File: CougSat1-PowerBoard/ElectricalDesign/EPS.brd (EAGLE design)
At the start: 90.4 x 95.8 mm, 416 parts, among them J1 Deployable 0, J11 CougSat Card, J2 PV1, J3 PV2, J5 SWD, J6 Umbilical, J7 PV0, J8 PV3, J9 Deployable 1, Q1 DMN53D0LDW, Q2 CSD25402Q3A, Q3 CSD25402Q3A, Q37 CSD25402Q3A, Q4 DMN2008LFU, Q5 CSD25402Q3A, Q6 DMN53D0LDW, Q8 DMN2008LFU, SW1 ESE24MH1, U1 TPS64200, U10 AD7689, U11 STM32L476RGT, U12 AD7689, U13 AD7291, U14 AD7291, U15 AD8515, U16 TPS64200, U17 AD8515, U18 INA199C1, U19 INA199C1, U2 AD7291, U20 BQ29700, U21 INA199C2, U22 INA199C1, U23 INA199C1, U24 INA199C1, U25 INA199C1, U26 TPS2115A, U27 TPS2115A, U28 TPS2115A, U29 TPS2115A, U3 AD7689, U30 TPS2115A, U31 TPS2115A, U32 TPS2115A, U33 TPS2115A, U34 TPS2115A, U35 TPS2115A, U36 TPS2115A, U37 TPS2115A, U38 TPS2115A, U39 TPS2115A, U4 TXS0102DQM, U40 TPS2115A, U41 TPS2115A, U42 TPS2115A, U43 TPS2115A, U44 TPS2115A, U45 TPS2115A, U46 TPS2115A, U47 TPS2115A, U48 TPS2115A, U49 TPS2115A, U5 TXS0102DQM, U50 TPS2115A, U51 AD8515, U52 TPS2115A, U53 TXS0102DQM, U54 TXS0102DQM, U55 TXS0102DQM, U6 BQ29700, U7 AD7291, U8 INA199C2, U9 AD7291, Y1 32.768kHz ±10ppm, Y2 8MHz ±10ppm

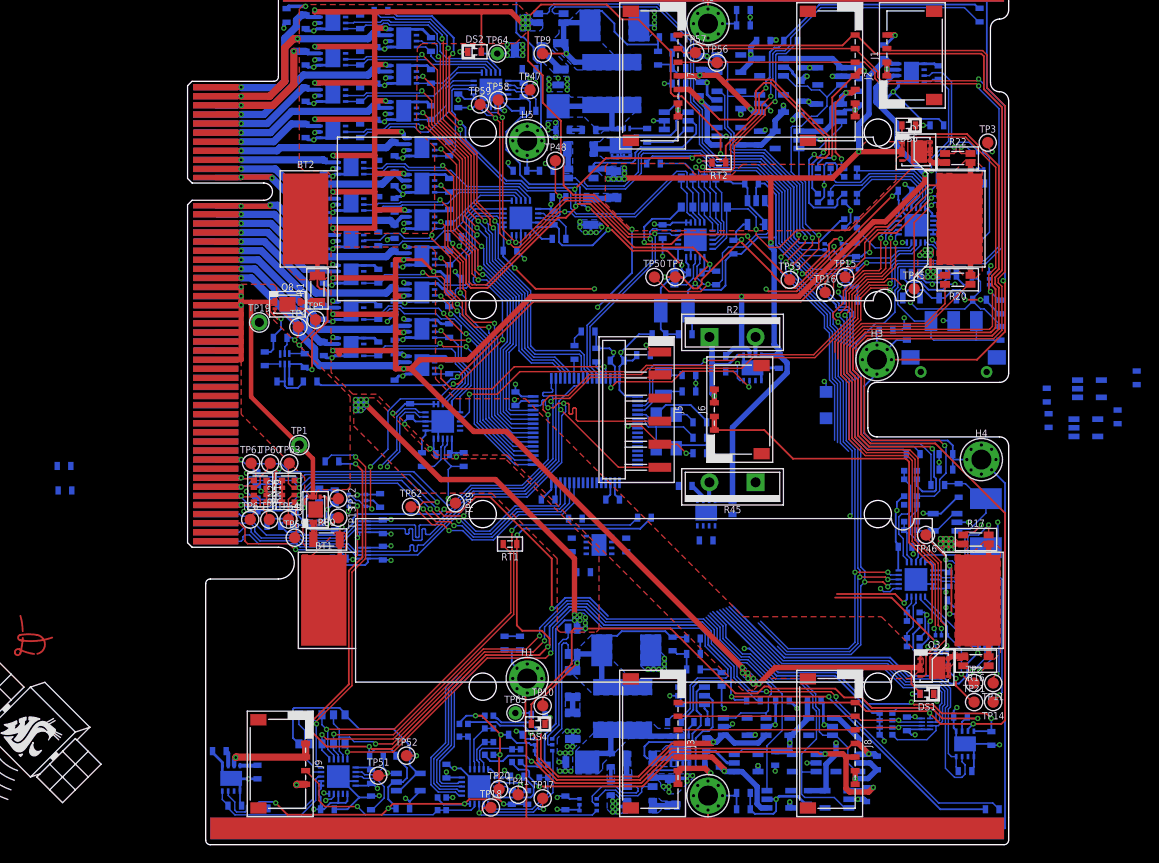
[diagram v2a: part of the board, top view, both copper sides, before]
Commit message: Laid out remaining signals
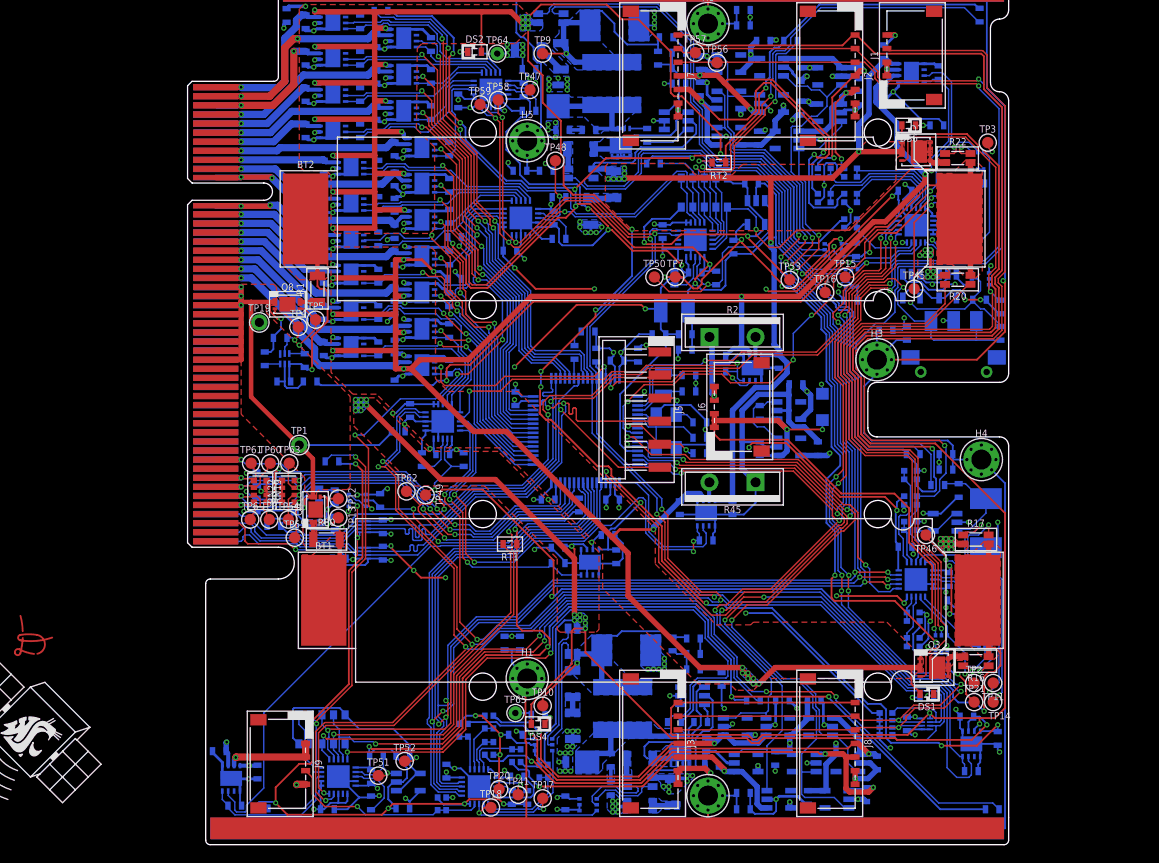
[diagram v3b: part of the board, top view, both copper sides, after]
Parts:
- moved R46 70.0 mm to (54.8, 6.60), turned to 0 degrees
- moved C60 37.5 mm to (67.0, 2.80), turned to 0 degrees
- moved R47 37.0 mm to (23.2, -2.40)
- moved D25 33.2 mm to (66.2, -0.10)
- moved C61 33.2 mm to (69.4, -4.30)
- moved D26 32.8 mm to (66.2, -4.10)
- moved C59 32.0 mm to (63.0, -4.30)
- moved R114 31.7 mm to (63.0, -0.30)
- moved R120 7.76 mm to (40.8, -16.9), turned to 0 degrees
- moved RT5 7.33 mm to (43.1, -10.5), turned to 90 degrees
- moved C65 6.16 mm to (47.2, -16.2), turned to 270 degrees
- moved C64 4.15 mm to (46.3, -13.8), turned to 180 degrees
- moved C66 3.89 mm to (40.8, -15.2), turned to 0 degrees
- moved TP49 3.42 mm to (26.2, -9.40)
- moved C73 2.47 mm to (54.2, -10.8), turned to 270 degrees
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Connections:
- removed net N$2: U7.3
- removed net N$3: U7.4
- removed net N$4: U7.5
- net !PC_3.3V-PV: now also U11.20
- net !PC_BH-1: now also U11.17
- net !PC_DEPLOY-0: now also U11.9
- net !PC_DEPLOY-1: now also U11.25
- net ADC_SEL-0: now also U11.24
- net ADC_SEL-2: now also U11.10
- net I_3.3V: now also U7.4
- net I_3.3V-PV: now also U7.5
- net I_BH-1: now also U7.3
- net PC_3.3V-5: now also U11.26
- net PC_PV-0/2A: now also U11.16
- net PC_PV-0/2B: now also U11.15
- net PC_PV-1/3A: now also U11.11
- net PC_PV-1/3B: now also U11.14
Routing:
- net PGND: track 979.6 -> 1146.2 mm, vias 122 -> 124
- net DGND: track 333.1 -> 468.7 mm, vias 20 -> 27
- net I2C_SDA: track 110.1 -> 225.8 mm, vias 5 -> 8
- net I2C_SCL: track 112.0 -> 224.7 mm, vias 5 -> 8
- net AVDD: track 237.4 -> 345.4 mm, vias 18 -> 22
- net 3.3V: track 320.4 -> 421.4 mm, vias 22 -> 29
- net SPI_MOSI: track 81.0 -> 156.0 mm, vias 4 -> 6
- net SPI_MISO: track 84.9 -> 157.5 mm, vias 4 -> 7
- net SPI_SCK: track 84.0 -> 154.9 mm
- net VBATT-B: track 261.3 -> 325.7 mm, vias 24 -> 26
- net !PC_DEPLOY-1: track 4.41 -> 64.0 mm
- net 3.3V-A: track 244.5 -> 303.0 mm, vias 24 -> 28
- net I_3.3V-PV: track 38.1 -> 95.1 mm, vias 0 -> 2
- net VBATT-A: track 260.2 -> 315.8 mm, vias 16 -> 17
- net PV_I2C_SCL: track 107.0 -> 162.2 mm, vias 3 -> 7
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
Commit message: Adjusted trace layout and polygons
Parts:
- moved LOGO2 99.1 mm to (81.0, -40.5)
- moved LOGO1 38.5 mm to (19.7, -24.7), flipped to the bottom
- moved RT12 1.14 mm to (16.6, -4.80)
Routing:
- net DB3: track 0.00 -> 48.4 mm
- net DB: track 0.00 -> 48.4 mm
- net PGND: track 1146.2 -> 1160.6 mm, vias 124 -> 136
- net DB5: track 0.00 -> 7.14 mm
- net DB4: track 0.00 -> 7.14 mm
- net VBATT-B: track 325.7 -> 331.7 mm, vias 26 -> 29
- net !VBATT_EN: track 97.2 -> 92.3 mm
- net 3.3V-B: track 233.8 -> 238.4 mm, vias 31 -> 35
- net PR_3.3V-0: track 72.1 -> 76.3 mm
- net I2C_SCL: track 224.7 -> 228.3 mm
- net I_BATT_IN-A_P: track 54.7 -> 51.6 mm
- net VBATT_EN: track 37.0 -> 40.0 mm
- net I_BATT_IN-A_N: track 55.8 -> 53.1 mm
- net 3.3V: track 421.4 -> 424.0 mm
- net CHASSIS: track 382.1 -> 384.3 mm
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- added copper zone on layer 15, net 3.3V
- added copper zone on layer 15, net 3.3V-A
- added copper zone on layer 2, net 3.3V-A
- added copper zone on layer 2, net AGND
- added copper zone on layer 15, net AVDD
- added copper zone on layer 15, net BALANCING-2
- added copper zone on layer 2, net BALANCING-2
- added copper zone on layer 1, net BALANCING-TOP
- added copper zone on layer 16, net BALANCING-TOP
- added copper zone on layer 1, net BP_VSS_I-A
- added copper zone on layer 1, net CHASSIS
- added copper zone on layer 15, net CHASSIS
- added copper zone on layer 16, net CHASSIS
- added copper zone on layer 2, net CHASSIS
- added copper zone on layer 2, net DB
- added copper zone on layer 2, net DB1
- added copper zone on layer 15, net DB2
- added copper zone on layer 15, net DB3
- added copper zone on layer 2, net DGND
- added copper zone on layer 15, net PGND
- added copper zone on layer 2, net PGND
- added copper zone on layer 16, net PR_3.3V-0
- added copper zone on layer 16, net PR_3.3V-1
- added copper zone on layer 16, net PR_3.3V-10
- added copper zone on layer 16, net PR_3.3V-11
- added copper zone on layer 16, net PR_3.3V-12
- added copper zone on layer 16, net PR_3.3V-2
- added copper zone on layer 16, net PR_3.3V-3
- added copper zone on layer 16, net PR_3.3V-4
- added copper zone on layer 16, net PR_3.3V-5
- added copper zone on layer 16, net PR_3.3V-6
- added copper zone on layer 16, net PR_3.3V-7
- added copper zone on layer 16, net PR_3.3V-8
- added copper zone on layer 16, net PR_3.3V-9
- added copper zone on layer 16, net PR_BATT-0
- added copper zone on layer 16, net PR_BATT-1
- added copper zone on layer 16, net PR_BATT-2
- added copper zone on layer 16, net PR_BATT-3
- added copper zone on layer 16, net PR_BATT-4
- added copper zone on layer 16, net PR_BATT-5
- added copper zone on layer 16, net PR_BATT-6
- added copper zone on layer 1, net PR_DEPLOY-0
- added copper zone on layer 1, net PR_DEPLOY-1
- added copper zone on layer 1, net UMB_IN

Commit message: Placed reference designators
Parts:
- removed C141, C149, C157, C163: 10µF 10%, CougsInSpace-Capacitors:1608
- removed C142, C145, C146, C150, C151, C158, C159, C164, C165, C169, C170, C171, C172, C173, C174: 100nF 10%, CougsInSpace-Capacitors:1608
- removed C148, C156, C162, C166: 1µF 10%, CougsInSpace-Capacitors:1608
- removed D24, D25, D26: MAX40200, CougsInSpace-DiscreteSemi:SOT23-5
- removed DS6: Green, CougsInSpace-LEDs:1608-POL
- removed J11: CougSat Card, CougsInSpace-Boards:CARD-FULL-OPEN+X
- removed Q37: CSD25402Q3A, CougsInSpace-DiscreteSemi:SON-3333
- removed R101: 150Ω 1%, CougsInSpace-Resistors:1608
- removed R102, R103, R90, R99: 0Ω <20mΩ, CougsInSpace-Resistors:1608
- removed R110: 10mΩ 1%, CougsInSpace-Resistors:3216
- removed R111: 12mΩ 1%, CougsInSpace-Resistors:3216-KELVIN
- removed R118: 1kΩ 0.1%, CougsInSpace-Resistors:1608
- removed R121, R122, R124, R126, R89: 2.2kΩ 1%, CougsInSpace-Resistors:1608
- removed R87: 620kΩ 1%, CougsInSpace-Resistors:1608
- removed R92: 360kΩ 1%, CougsInSpace-Resistors:1608
- removed RN22: 10kΩ 1%, CougsInSpace-Resistors:1632
- removed TP45, TP47, TP48, TP50, TP53, TP56, TP57, TP58, TP59, TP60, TP61: TEST_POINT-SMD-C-1.25, CougsInSpace-Connectors:SMD-C-1.25
- removed TP64: TEST_POINT-THT-0.7, CougsInSpace-Connectors:THT-0.7
- added C100, C104, C106, C109, C75, C76, C77, C81, C83, C90: 100nF 10%, CougsInSpace-Capacitors:1608
- added C101, C102, C110, C74, C78, C79, C82, C84, C86, C88: 10µF 10%, CougsInSpace-Capacitors:1608
- added C80: 4.7µF 10%, CougsInSpace-Capacitors:4028-POL
- added C85: 1µF 10%, CougsInSpace-Capacitors:1608
- added C99: 10µF 10%, CougsInSpace-Capacitors:3216
- added D2, D5: MAX40200, CougsInSpace-DiscreteSemi:SOT23-5
- added D6: MBRM120LT, CougsInSpace-DiscreteSemi:POWERMITE
- added DS5: Green, CougsInSpace-LEDs:1608-POL
- added J4: Umbilical, CougsInSpace-Connectors:PICOLOCK1.5-04
- added Q7: DMN53D0LDW, CougsInSpace-DiscreteSemi:SOT363
- added R27: 330Ω 1%, CougsInSpace-Resistors:1608
- added R28, R30, R40: 4.75MΩ 1%, CougsInSpace-Resistors:1608
- added R34, R44, R48, R66, R75: 0Ω <20mΩ, CougsInSpace-Resistors:1608
- added R42, R49: 1kΩ 0.1%, CougsInSpace-Resistors:1608
- added R51, R54: 2.2kΩ 1%, CougsInSpace-Resistors:1608
- added R64: 10mΩ 1%, CougsInSpace-Resistors:3216
- added R82: 12mΩ 1%, CougsInSpace-Resistors:3216-KELVIN
- added RN21: 5kΩ 0.1%, CougsInSpace-Resistors:1616
- added TP25, TP26, TP27, TP28, TP32, TP33, TP34, TP35, TP36, TP40, TP42, TP43: TEST_POINT-SMD-C-1.25, CougsInSpace-Connectors:SMD-C-1.25
- C1, C13, C16, C2, C32, C40: value 10µF 10% -> 100nF 10%; device CougsInSpace-Capacitors:3216 -> CougsInSpace-Capacitors:1608
- C10, C36: value 8pF ±0.25 -> 100nF 10%
- C105, C11, C26, C3: value 100nF 10% -> 10µF 10%; device CougsInSpace-Capacitors:1608 -> CougsInSpace-Capacitors:3216
- C108, C111, C115, C7, C70, C93, C96: value 100nF 10% -> 10µF 10%
- C112, C117, C18, C23, C29, C6, C67, C9: value 100nF 10% -> 1µF 10%
- C114, C12: value 100nF 10% -> 470pF 1%
- C116, C119, C123, C125, C126, C128, C134, C20: value 10µF 10% -> 1µF 10%
- C121, C122, C132, C136, C139, C24, C64: value 10µF 10% -> 100nF 10%
- C129: value 10µF 10% -> 4.7pF ±0.1
- C131, C133: device CougsInSpace-Capacitors:1608 -> CougsInSpace-Capacitors:3216
- C137: value 15pF 1% -> 220µF 10%; device CougsInSpace-Capacitors:1608 -> CougsInSpace-Capacitors:7132-POL
- C138: value 15pF 1% -> 10µF 10%
- C15: value 4.7pF ±0.1 -> 100nF 10%
- C17: value 220µF 10% -> 1µF 10%; device CougsInSpace-Capacitors:7132-POL -> CougsInSpace-Capacitors:1608
- C21: value 10nF 10% -> 10µF 10%
- C30: value 4.7pF ±0.1 -> 1µF 10%
- C31: value 220µF 10% -> 10µF 10%; device CougsInSpace-Capacitors:7132-POL -> CougsInSpace-Capacitors:3216
- C33: value 10µF 10% -> 220µF 10%; device CougsInSpace-Capacitors:3216 -> CougsInSpace-Capacitors:7132-POL
- C34: value 100nF 10% -> 4.7pF ±0.1
- C37: value 470pF 1% -> 100nF 10%
- C39: device CougsInSpace-Capacitors:3216 -> CougsInSpace-Capacitors:1608
- C4: value 4.7µF 10% -> 100nF 10%; device CougsInSpace-Capacitors:4028-POL -> CougsInSpace-Capacitors:1608
- C43, C44, C46, C48, C49, C50, C51, C52, C53, C54, C55, C58: value 1µF 10% -> 100nF 10%
- C45, C56: value 1µF 10% -> 10µF 10%
- C47: value 1µF 10% -> 220µF 10%; device CougsInSpace-Capacitors:1608 -> CougsInSpace-Capacitors:7132-POL
- C5: value 470pF 1% -> 1µF 10%
- C59: value 1µF 10% -> 10nF 10%
- C62: value 220µF 10% -> 8pF ±0.25; device CougsInSpace-Capacitors:7132-POL -> CougsInSpace-Capacitors:1608
- C63: value 100nF 10% -> 8pF ±0.25
- C66, C69: value 100nF 10% -> 15pF 1%
- D1, D8: value MBRM120LT -> MAX40200; device CougsInSpace-DiscreteSemi:POWERMITE -> CougsInSpace-DiscreteSemi:SOT23-5
- D12: value MAX40200 -> SS1FH10; device CougsInSpace-DiscreteSemi:SOT23-5 -> CougsInSpace-DiscreteSemi:DO-219AB
- D18: value MAX40200 -> MBRM120LT; device CougsInSpace-DiscreteSemi:SOT23-5 -> CougsInSpace-DiscreteSemi:POWERMITE
- D3: value SS1FH10 -> MAX40200; device CougsInSpace-DiscreteSemi:DO-219AB -> CougsInSpace-DiscreteSemi:SOT23-5
- J2: value PV1 -> PV0
- J3: value PV2 -> PV1
- J5: value SWD -> CougSat Card; device CougsInSpace-Connectors:SMD2.54-1X06-R -> CougsInSpace-Boards:CARD-FULL-OPEN+X
- J6: value Umbilical -> SWD; device CougsInSpace-Connectors:PICOLOCK1.5-04 -> CougsInSpace-Connectors:SMD2.54-1X06-R
- J7: value PV0 -> PV2
- LOGO1: value Satellite 16mm -> SIGNATUREBRADLEY; device CougsInSpace-Aesthetics:CIS-SATELLITE-16 -> CougsInSpace-Aesthetics:SIGN-BRADLEY
- LOGO2: value SIGNATUREBRADLEY -> Satellite 16mm; device CougsInSpace-Aesthetics:SIGN-BRADLEY -> CougsInSpace-Aesthetics:CIS-SATELLITE-16
- Q1: value DMN53D0LDW -> CSD25402Q3A; device CougsInSpace-DiscreteSemi:SOT363 -> CougsInSpace-DiscreteSemi:SON-3333
- Q2, Q3: value CSD25402Q3A -> DMN2008LFU; device CougsInSpace-DiscreteSemi:SON-3333 -> CougsInSpace-DiscreteSemi:UDFN-6-B
- Q4, Q8: value DMN2008LFU -> CSD25402Q3A; device CougsInSpace-DiscreteSemi:UDFN-6-B -> CougsInSpace-DiscreteSemi:SON-3333
- R1: value 10mΩ 1% -> 12mΩ 1%; device CougsInSpace-Resistors:3216 -> CougsInSpace-Resistors:3216-KELVIN
- R10: value 0Ω <20mΩ -> 470Ω 0.5%
- R11, R61: value 1kΩ 0.1% -> 12mΩ 1%; device CougsInSpace-Resistors:1608 -> CougsInSpace-Resistors:3216-KELVIN
- R12: value 150Ω 1% -> 2.2kΩ 1%
- R13: value 2.2kΩ 1% -> 150Ω 1%
- R14: value 1kΩ 0.1% -> 10mΩ 1%; device CougsInSpace-Resistors:1608 -> CougsInSpace-Resistors:3216
- R15: value 12mΩ 1% -> 0Ω <20mΩ; device CougsInSpace-Resistors:3216-KELVIN -> CougsInSpace-Resistors:1608
- R16, R17: value 12mΩ 1% -> 1kΩ 0.1%; device CougsInSpace-Resistors:3216-KELVIN -> CougsInSpace-Resistors:1608
- R18: value 0Ω <20mΩ -> 360kΩ 1%
- R19: value 360kΩ 1% -> 0Ω <20mΩ
- R2: value 10Ω 5% -> 12mΩ 1%; device CougsInSpace-Resistors:TO-220-2 -> CougsInSpace-Resistors:3216-KELVIN
- R20: value 12mΩ 1% -> 620kΩ 1%; device CougsInSpace-Resistors:3216-KELVIN -> CougsInSpace-Resistors:1608
- R21: value 4.75MΩ 1% -> 0Ω <20mΩ
- R25: value 330Ω 1% -> 10kΩ 0.1%
- R26: value 0Ω <20mΩ -> 750Ω 0.5%
- R29: value 2.2kΩ 1% -> 10kΩ 0.1%
- R3: value 4.75MΩ 1% -> 10mΩ 1%; device CougsInSpace-Resistors:1608 -> CougsInSpace-Resistors:3216
- R31: value 620kΩ 1% -> 2.2kΩ 1%
- R37: value 1kΩ 0.1% -> 330Ω 1%
- R38, R39: value 1kΩ 0.1% -> 750Ω 0.5%
- R4: value 4.75MΩ 1% -> 10Ω 5%; device CougsInSpace-Resistors:1608 -> CougsInSpace-Resistors:TO-220-2
- R41: value 12mΩ 1% -> 2.2kΩ 1%; device CougsInSpace-Resistors:3216-KELVIN -> CougsInSpace-Resistors:1608
- R43, R62: value 2.2kΩ 1% -> 0Ω <20mΩ
- R45: value 10Ω 5% -> 750Ω 0.5%; device CougsInSpace-Resistors:TO-220-2 -> CougsInSpace-Resistors:1608
- R46: value 0Ω <20mΩ -> 4.75MΩ 1%
- R47: value 0Ω <20mΩ -> 1kΩ 0.1%
- R5: value 12mΩ 1% -> 10Ω 5%; device CougsInSpace-Resistors:3216-KELVIN -> CougsInSpace-Resistors:TO-220-2
- R50, R55, R73: value 0Ω <20mΩ -> 2.2kΩ 1%
- R56: value 330Ω 1% -> 1kΩ 0.1%
- R58: value 2.2kΩ 1% -> 750Ω 0.5%
- R60, R65: value 750Ω 0.5% -> 2.2kΩ 1%
- R67: value 750Ω 0.5% -> 1.2kΩ 0.1%
- R68: value 470Ω 0.5% -> 150Ω 1%
- R69: value 470Ω 0.5% -> 1kΩ 0.1%
- R7, R8: value 10kΩ 0.1% -> 12mΩ 1%; device CougsInSpace-Resistors:1608 -> CougsInSpace-Resistors:3216-KELVIN
- R70: value 1.2kΩ 0.1% -> 2.2kΩ 1%
- R72: value 2.2kΩ 1% -> 360kΩ 1%
- R74: value 750Ω 0.5% -> 470Ω 0.5%
- R77: value 1kΩ 0.1% -> 620kΩ 1%
- R78: value 2.2kΩ 1% -> 1kΩ 0.1%
- R79: value 4.75MΩ 1% -> 2.2kΩ 1%
- R80: value 10mΩ 1% -> 0Ω <20mΩ; device CougsInSpace-Resistors:3216 -> CougsInSpace-Resistors:1608
- R83: value 750Ω 0.5% -> 0Ω <20mΩ
- RN1, RN2, RN9: value 5kΩ 0.1% -> 10kΩ 1%; device CougsInSpace-Resistors:1616 -> CougsInSpace-Resistors:1632
- RN17, RN18: value 10kΩ 5% -> 5kΩ 0.1%; device CougsInSpace-Resistors:3264 -> CougsInSpace-Resistors:1616
- RN19: value 10kΩ 1% -> 10kΩ 5%; device CougsInSpace-Resistors:1632 -> CougsInSpace-Resistors:3264
- RN20: value 10kΩ 1% -> 5kΩ 0.1%; device CougsInSpace-Resistors:1632 -> CougsInSpace-Resistors:1616
- RN8: value 5kΩ 0.1% -> 10kΩ 5%; device CougsInSpace-Resistors:1616 -> CougsInSpace-Resistors:3264
- TP1: value TEST_POINT-THT-1.0 -> TEST_POINT-SMD-C-1.25; device CougsInSpace-Connectors:THT-1.0 -> CougsInSpace-Connectors:SMD-C-1.25
- TP17: value TEST_POINT-SMD-C-1.25 -> TEST_POINT-THT-1.0; device CougsInSpace-Connectors:SMD-C-1.25 -> CougsInSpace-Connectors:THT-1.0
- TP2: value TEST_POINT-SMD-C-1.25 -> TEST_POINT-THT-0.7; device CougsInSpace-Connectors:SMD-C-1.25 -> CougsInSpace-Connectors:THT-0.7
- U1: value TPS64200 -> INA199C1; device CougsInSpace-IC-Power:SOT23-6 -> CougsInSpace-IC-Amplifiers:SOT363
- U10: value AD7689 -> INA199C2; device CougsInSpace-IC-Conversion:QFN-20-4040 -> CougsInSpace-IC-Amplifiers:SOT363
- U11: value STM32L476RGT -> INA199C1; device CougsInSpace-IC-µController:QFP-64-1010 -> CougsInSpace-IC-Amplifiers:SOT363
- U13: value AD7291 -> INA199C2; device CougsInSpace-IC-Conversion:QFN-20-4040 -> CougsInSpace-IC-Amplifiers:SOT363
- U14, U7: value AD7291 -> TPS2115A; device CougsInSpace-IC-Conversion:QFN-20-4040 -> CougsInSpace-IC-Power:VSON-8
- U15: value AD8515 -> TXS0102DQM; device CougsInSpace-IC-Amplifiers:SOT23-5 -> CougsInSpace-IC-Comms:X2SON-8
- U16: value TPS64200 -> TXS0102DQM; device CougsInSpace-IC-Power:SOT23-6 -> CougsInSpace-IC-Comms:X2SON-8
- U18: value INA199C1 -> BQ29700; device CougsInSpace-IC-Amplifiers:SOT363 -> CougsInSpace-IC-Power:WSON-6
- U19, U24, U25: value INA199C1 -> TPS2115A; device CougsInSpace-IC-Amplifiers:SOT363 -> CougsInSpace-IC-Power:VSON-8
- U2: value AD7291 -> AD7689
- U20: value BQ29700 -> TXS0102DQM; device CougsInSpace-IC-Power:WSON-6 -> CougsInSpace-IC-Comms:X2SON-8
- U21, U8: value INA199C2 -> TXS0102DQM; device CougsInSpace-IC-Amplifiers:SOT363 -> CougsInSpace-IC-Comms:X2SON-8
- U22: value INA199C1 -> STM32L476RGT; device CougsInSpace-IC-Amplifiers:SOT363 -> CougsInSpace-IC-µController:QFP-64-1010
- U23: value INA199C1 -> AD7291; device CougsInSpace-IC-Amplifiers:SOT363 -> CougsInSpace-IC-Conversion:QFN-20-4040
- U26: value TPS2115A -> BQ29700; device CougsInSpace-IC-Power:VSON-8 -> CougsInSpace-IC-Power:WSON-6
- U3: value AD7689 -> AD8515; device CougsInSpace-IC-Conversion:QFN-20-4040 -> CougsInSpace-IC-Amplifiers:SOT23-5
- U31, U34, U44: value TPS2115A -> INA199C1; device CougsInSpace-IC-Power:VSON-8 -> CougsInSpace-IC-Amplifiers:SOT363
- U35, U39, U50: value TPS2115A -> AD7291; device CougsInSpace-IC-Power:VSON-8 -> CougsInSpace-IC-Conversion:QFN-20-4040
- U37: value TPS2115A -> AD7689; device CougsInSpace-IC-Power:VSON-8 -> CougsInSpace-IC-Conversion:QFN-20-4040
- U4, U53, U54, U55: value TXS0102DQM -> TPS2115A; device CougsInSpace-IC-Comms:X2SON-8 -> CougsInSpace-IC-Power:VSON-8
- U40: value TPS2115A -> AD8515; device CougsInSpace-IC-Power:VSON-8 -> CougsInSpace-IC-Amplifiers:SOT23-5
- U47: value TPS2115A -> TPS64200; device CougsInSpace-IC-Power:VSON-8 -> CougsInSpace-IC-Power:SOT23-6
- U5: value TXS0102DQM -> AD7291; device CougsInSpace-IC-Comms:X2SON-8 -> CougsInSpace-IC-Conversion:QFN-20-4040
- U51: value AD8515 -> TPS2115A; device CougsInSpace-IC-Amplifiers:SOT23-5 -> CougsInSpace-IC-Power:VSON-8
- U6: value BQ29700 -> INA199C1; device CougsInSpace-IC-Power:WSON-6 -> CougsInSpace-IC-Amplifiers:SOT363
- U9: value AD7291 -> TPS64200; device CougsInSpace-IC-Conversion:QFN-20-4040 -> CougsInSpace-IC-Power:SOT23-6
- Y1: value 32.768kHz ±10ppm -> 8MHz ±10ppm; device CougsInSpace-Clocks:SMD-3215 -> CougsInSpace-Clocks:SMD-5032
- Y2: value 8MHz ±10ppm -> 32.768kHz ±10ppm; device CougsInSpace-Clocks:SMD-5032 -> CougsInSpace-Clocks:SMD-3215
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- renumbered C140 to C92, C143 to C97, C152 to C94, C153 to C103, C154 to C89, C155 to C98, C160 to C95, C161 to C87, C167 to C91, C168 to C107, R114 to R36, R115 to R32, R116 to R33, R117 to R53, R120 to R24, R123 to R76, R125 to R71, R84 to R23, R85 to R57, R88 to R52, TP46 to TP30, TP49 to TP24, TP51 to TP39, TP52 to TP38, TP54 to TP29, TP55 to TP31, TP62 to TP23, TP63 to TP22, TP65 to TP37
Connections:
- net !NRST: now also C59.1, J6.5, U22.7; no longer C21.1, J5.5, U11.7
- net !PC_3.3V-0: now also U22.57, U55.3; no longer U11.57, U27.3
- net !PC_3.3V-1: now also U22.56, U54.3; no longer U11.56, U28.3
- net !PC_3.3V-10: now also U22.41, U41.3; no longer U11.41, U37.3
- net !PC_3.3V-11: now also U22.39; no longer U11.39
- net !PC_3.3V-12: now also U22.40, U36.3; no longer U11.40, U39.3
- net !PC_3.3V-2: now also U22.53, U53.3; no longer U11.53, U29.3
- net !PC_3.3V-3: now also U22.52, U51.3; no longer U11.52, U30.3
- net !PC_3.3V-4: now also U22.51, U49.3; no longer U11.51, U31.3
- net !PC_3.3V-5: now also U48.3; no longer U32.3
- net !PC_3.3V-6: now also U22.45, U46.3; no longer U11.45, U33.3
- net !PC_3.3V-7: now also U22.44, U45.3; no longer U11.44, U34.3
- net !PC_3.3V-8: now also U22.43, U43.3; no longer U11.43, U35.3
- net !PC_3.3V-9: now also U22.42, U42.3; no longer U11.42, U36.3
- net !PC_3.3V-PV: now also U22.20, U7.3; no longer U11.20, U52.3
- net !PC_BATT-0: now also U22.38, U33.3; no longer U11.38, U40.3
- net !PC_BATT-1: now also U22.37, U32.3; no longer U11.37, U41.3
- net !PC_BATT-2: now also U22.36, U30.3; no longer U11.36, U42.3
- net !PC_BATT-3: now also U22.35, U29.3; no longer U11.35, U43.3
- net !PC_BATT-4: now also U22.34, U28.3; no longer U11.34, U44.3
- net !PC_BATT-5: now also U22.33, U27.3; no longer U11.33, U45.3
- net !PC_BATT-6: now also U22.61, U25.3; no longer U11.61, U46.3
- net !PC_BH-0: now also U22.62, U24.3; no longer U11.62, U47.3
- net !PC_BH-1: now also U19.3, U22.17; no longer U11.17, U48.3
- net !PC_DEPLOY-0: now also U22.9, U52.3; no longer U11.9, U49.3
- net !PC_DEPLOY-1: now also U22.25, U4.3; no longer U11.25, U50.3
- net !VBATT_EN: now also Q1.4, Q4.4, Q7.2, Q7.3; no longer Q1.2, Q1.3, Q2.4, Q3.4
- net 3.3V: now also C1.1, C104.1, C118.1, C16.1, C42.1, C44.1, C45.1, C46.1, C51.1, C52.1, C53.1, C54.1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; no longer C145.1, C150.1, C158.1, C164.1, C172.1, C173.1, C174.1, C23.1, C25.1, C26.1, C41.1, C6.1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
- net 3.3V-A: now also C100.1, C24.1, C41.1, DS1.A, R82.2, RN16.2, U14.8, U41.8, U42.8, U43.8, U45.8, U46.8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; no longer C117.1, C65.1, C68.1, DS2.A, R41.2, RN7.2, U26.8, U27.8, U28.8, U29.8, U30.8, U31.8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
- net 3.3V-B: now also C139.1, C28.1, C43.1, R22.1, RN4.2, U14.6, U41.6, U42.6, U43.6, U45.6, U46.6, U48.6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; no longer C118.1, C66.1, C67.1, R15.1, RN12.2, U26.6, U27.6, U28.6, U29.6, U30.6, U31.6, U32.6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
- net 3.3V_I-A: now also C129.1, C131.1, C137.A, L2.2, R80.2, R82.1, TP3.1; no longer C13.1, C15.1, C17.A, L1.2, R35.2, R41.1, TP9.1
- net 3.3V_I-B: now also C31.1, C33.A, C34.1, L1.2, R22.2, TP36.1; no longer C30.1, C31.A, C33.1, L2.2, R15.2, TP10.1
- net 3.3V_ISENS-A: now also Q8.5, Q8.6, Q8.7, Q8.8, Q8.PAD, R64.1, U47.4; no longer Q5.5, Q5.6, Q5.7, Q5.8, Q5.PAD, R6.1, U1.4
- net 3.3V_ISENS-B: now also Q5.5, Q5.6, Q5.7, Q5.8, Q5.PAD, R14.1, U9.4; no longer Q37.5, Q37.6, Q37.7, Q37.8, Q37.PAD, R110.1, U16.4
- net 3.3V_LED-A: now also DS1.C, R78.2; no longer DS2.C, R38.2
- net 3.3V_LED-B: now also R16.2; no longer R77.2
- net 3.3V_REG_BUCK_NODE-A: now also D18.C, L2.1, Q8.1, Q8.2, Q8.3, R68.2; no longer D1.C, L1.1, Q5.1, Q5.2, Q5.3, R12.2
- net 3.3V_REG_BUCK_NODE-B: now also D6.C, L1.1, Q5.1, Q5.2, Q5.3, R13.2; no longer D8.C, L2.1, Q37.1, Q37.2, Q37.3, R101.2
- net 3.3V_REG_FB-A: now also C129.2, R75.2, R77.1, U47.3; no longer C15.2, R26.2, R31.1, U1.3
- net 3.3V_REG_FB-B: now also C34.2, R19.2, R20.1, U9.3; no longer C30.2, R87.1, R90.2, U16.3
- net 3.3V_REG_FBRES_HIGH-A: now also R77.2, R80.1; no longer R31.2, R35.1
- net 3.3V_REG_FBRES_HIGH-B: now also R20.2; no longer R87.2
- net 3.3V_REG_FBRES_LOW-A: now also R72.2, R75.1; no longer R19.2, R26.1
- net 3.3V_REG_FBRES_LOW-B: now also R18.2, R19.1; no longer R90.1, R92.2
- net 3.3V_REG_INCAP-A: now also C105.2, C99.1; no longer C1.2, C2.1
- net 3.3V_REG_INCAP-B: now also C11.2, C3.1; no longer C39.1, C40.2
- net 3.3V_REG_OUTCAP-A: now also C131.2, C133.1; no longer C13.2, C16.1
- net 3.3V_REG_OUTCAP-B: now also C26.1, C31.2; no longer C32.1, C33.2
- net 3.3V_REG_RSENS-A: now also R61.1, R64.2; no longer R5.1, R6.2
- net 3.3V_REG_RSENS-B: now also R11.1, R14.2; no longer R110.2, R111.1
- net 3.3V_REG_SNUBBER-A: now also C114.1, R68.1; no longer C5.1, R12.1
- net 3.3V_REG_SNUBBER-B: now also C12.1, R13.1; no longer C37.1, R101.1
- net 3.3V_REG_SW-A: now also R66.1, U47.6; no longer R9.1, U1.6
- net 3.3V_REG_SW-B: now also R15.1, U9.6; no longer R102.1, U16.6
- net 3.3V_REG_SW_GATE-A: now also Q8.4, R66.2; no longer Q5.4, R9.2
- net 3.3V_REG_SW_GATE-B: now also Q5.4, R15.2; no longer Q37.4, R102.2
- net ADC_3.3V-A: now also RN16.3, RN16.4, U37.9; no longer RN7.3, RN7.4, U10.9
- net ADC_3.3V-B: now also RN4.3, RN4.4, U2.6; no longer RN12.3, RN12.4, U3.6
- net ADC_DCAP-3: now also C116.1, U50.8; no longer C148.1, U13.8
- net ADC_DCAP-4: now also U39.8; no longer U2.8
- net ADC_DCAP-5: now also C57.1, U23.8; no longer C156.1, U7.8
- net ADC_DCAP-6: now also C85.1, U35.8; no longer C19.1, U9.8
- net ADC_DCAP-7: now also C5.1, U5.8; no longer C162.1, U14.8
- net ADC_EJECT_TIMER_BUF: now also RN13.3, RN13.4; no longer RN8.3, RN8.4
- net ADC_PV_IN-0A: now also RN17.3, RN17.4, U37.16; no longer RN2.3, RN2.4, U10.16
- net ADC_PV_IN-0B: now also RN18.3, RN18.4, U37.17; no longer RN3.3, RN3.4, U10.17
- net ADC_PV_IN-1A: now also RN21.3, RN21.4, U37.18; no longer RN4.3, RN4.4, U10.18
- net ADC_PV_IN-1B: now also RN20.3, RN20.4, U37.19; no longer RN5.3, RN5.4, U10.19
- net ADC_PV_IN-2A: now also U2.17; no longer U3.17
- net ADC_PV_IN-2B: now also RN5.3, RN5.4, U2.19; no longer RN11.3, RN11.4, U3.19
- net ADC_PV_IN-3A: now also RN7.3, RN7.4, U2.16; no longer RN13.3, RN13.4, U3.16
- net ADC_PV_IN-3B: now also RN6.3, RN6.4, U2.18; no longer RN9.3, RN9.4, U3.18
- net ADC_REF-0: now also C7.1, U2.2; no longer C24.1, U3.2
- net ADC_REF-1: now also C102.1, TP14.1, U37.2; no longer C139.1, TP45.1, U10.2
- net ADC_REF-2: now also C39.1; no longer C141.1
- net ADC_REF-3: now also C127.1, TP5.1, U50.7; no longer C149.1, TP47.1, U13.7
- net ADC_REF-4: now also TP9.1, U39.7; no longer TP48.1, U2.7
- net ADC_REF-5: now also C56.1, U23.7; no longer C157.1, U7.7
- net ADC_REF-6: now also C84.1, TP10.1, U35.7, U40.3; no longer C20.1, TP50.1, U51.3, U9.7
- net ADC_REF-7: now also C21.1, U3.3, U5.7; no longer C163.1, U14.7, U15.3
- net ADC_REFIN-0: now also C8.1, U2.3; no longer C42.1, U3.3
- net ADC_REFIN-1: now also U37.3; no longer U10.3
- net ADC_REFIN-2: now also C37.1; no longer C142.1
- net ADC_SEL-0: now also U2.11, U22.24; no longer U11.24, U3.11
- net ADC_SEL-1: now also U22.2, U37.11; no longer U10.11, U11.2
- net ADC_SEL-2: now also U22.10; no longer U11.10
- net ADC_UMB_IN: now also RN11.3, RN11.4; no longer RN14.3, RN14.4
- net ADC_VBATT-A: now also RN15.3, RN15.4; no longer RN6.3, RN6.4
- net ADC_VBATT-B: now also RN12.3, RN12.4; no longer RN1.3, RN1.4
- net AGND: now also C102.2, C106.2, C14.2, C2.2, C21.2, C25.2, C32.2, C36.2, C37.2, C38.2, C39.2, C4.2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; no longer C139.2, C141.2, C142.2, C157.2, C159.2, C163.2, C165.2, C166.2, C169.2, C170.2, C171.2, C18.2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
- net AVDD: now also C106.1, C122.1, C13.1, C14.1, C2.1, C25.1, C32.1, C36.1, C38.1, C4.1, C40.1, C58.1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; no longer C12.1, C146.1, C151.1, C159.1, C165.1, C169.1, C170.1, C171.1, C18.1, C29.1, C3.1, C34.1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
- net AVREF-0: now also RN19.10, RN19.5, TP13.1, U40.1, U40.4; no longer RN18.10, RN18.5, TP53.1, U51.1, U51.4
- net AVREF-1: now also C20.1, RN8.10, RN8.5, U3.1, U3.4; no longer C166.1, RN17.10, RN17.5, U15.1, U15.4
- net BATT_PROTECT_BAT-A: now also C68.1, R37.1, U26.5; no longer C14.1, R25.1, U6.5
- net BATT_PROTECT_BAT-B: now also C48.1, R27.1, U18.5; no longer C63.1, R56.1, U20.5
- net BATT_PROTECT_COUT-A: now also Q2.3, R46.2, TP18.1, U26.2; no longer Q8.3, R21.2, TP4.1, U6.2
- net BATT_PROTECT_COUT-B: now also Q3.4, R30.2, TP25.1, U18.2; no longer Q4.4, R79.2, TP12.1, U20.2
- net BATT_PROTECT_DOUT-A: now also Q2.4, R40.1, TP16.1, U26.3; no longer Q8.4, R3.1, TP5.1, U6.3
- net BATT_PROTECT_DOUT-B: now also Q3.3, R28.2, TP26.1, U18.3; no longer Q4.3, R4.2, TP13.1, U20.3
- net BATT_PROTECT_GND-A: now also R41.2, U26.6; no longer R29.2, U6.6
- net BATT_PROTECT_GND-B: now also R31.2, U18.6; no longer R62.2, U20.6
- net BOOT0: now also R43.2, U22.60; no longer R55.2, U11.60
- net BP_VSS-A: now also BT1.A, C68.2, R40.2, U26.4; no longer BT2.A, C14.2, R1.2, U6.4
- net BP_VSS-A1: now also BT2.A, C48.2, R28.1, R6.2, U18.4; no longer BT1.A, C63.2, R4.1, R80.2, U20.4
- net BP_VSS_I-A: now also Q2.6, R3.1; no longer Q8.6, R1.1
- net BP_VSS_I-B: now also Q3.1, R6.1; no longer Q4.1, R80.1
- net BUS_CTRL_SYNC: now also J5.A42, J5.B42, RN1.1, TP20.1, U21.3; no longer J11.A42, J11.B42, RN19.1, TP61.1, U55.3
- net BUS_I2C0_IRQ: now also J5.A45, J5.B45, RN1.4, TP27.1, U20.2; no longer J11.A45, J11.B45, RN19.4, TP6.1, U54.2
- net BUS_I2C0_SCL: now also J5.A44, J5.B44, RN1.3, TP28.1, U20.3; no longer J11.A44, J11.B44, RN19.3, TP8.1, U54.3
- net BUS_I2C0_SDA: now also J5.A43, J5.B43, RN1.2, TP21.1, U21.2; no longer J11.A43, J11.B43, RN19.2, TP60.1, U55.2
- net BUS_I2C_IRQ: now also RN2.1, U20.7, U22.28; no longer RN22.1, U11.28, U54.7
- net BUS_I2C_SCL: now also RN2.2, U20.6, U22.29; no longer RN22.2, U11.29, U54.6
- net BUS_I2C_SDA: now also RN2.3, U21.7, U22.30; no longer RN22.3, U11.30, U55.7
- net BUS_JTAG_TCK: now also J5.A46, U16.7; no longer J11.A46, U5.7
- net BUS_JTAG_TDI: now also J5.A47, U16.6; no longer J11.A47, U5.6
- net BUS_JTAG_TDO: now also J5.A48, U15.7; no longer J11.A48, U4.7
- net BUS_JTAG_TMS: now also J5.A49, U15.6; no longer J11.A49, U4.6
- net CHASSIS: now also C10.1, C109.1, C136.1, C55.1, C77.1, J5.CHASSIS@1, J5.CHASSIS@2, J5.CHASSIS@3, J5.CHASSIS@4, R21.2, R34.2, R48.2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; no longer C11.1, C22.1, C28.1, C38.1, C9.1, J11.CHASSIS@1, J11.CHASSIS@2, J11.CHASSIS@3, J11.CHASSIS@4, R10.2, R103.2, R18.2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
- net CTRL_SYNC: now also RN2.4, U21.6, U22.27; no longer RN22.4, U11.27, U55.6
- net DEPLOY_SENSE-0: now also RN14.3, RN14.4; no longer RN15.3, RN15.4
- net DEPLOY_SENSE-1: now also RN3.3, RN3.4, U2.9; no longer RN16.3, RN16.4, U3.9
- net DGND: now also C1.2, C104.2, C116.2, C118.2, C13.2, C16.2, C40.2, C42.2, C44.2, C46.2, C5.2, C51.2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; no longer C10.2, C12.2, C137.2, C138.2, C145.2, C146.2, C148.2, C150.2, C156.2, C158.2, C162.2, C164.2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
- net EJECT_TIMER: now also C47.A; no longer C62.A
- net EJECT_TIMER_BUF: now also RN13.2; no longer RN8.2
- net EJECT_TIMER_DISCHARGE: now also Q7.6; no longer Q1.6
- net I2C_SCL: now also RN9.4, TP7.1, U22.58, U23.15, U35.15, U39.15, U5.15, U50.15, U8.7; no longer RN20.4, TP59.1, U11.58, U13.15, U14.15, U2.15, U53.7, U7.15, U9.15
- net I2C_SDA: now also RN9.1, TP6.1, U22.59, U23.14, U35.14, U39.14, U5.14, U50.14, U8.6; no longer RN20.1, TP58.1, U11.59, U13.14, U14.14, U2.14, U53.6, U7.14, U9.14
- net I_3.3V: now also U14.4, U23.4; no longer U26.4, U7.4
- net I_3.3V-0: now also R81.2, U50.5, U55.4; no longer R121.2, U13.5, U27.4
- net I_3.3V-1: now also R79.2, U50.4, U54.4; no longer R122.2, U13.4, U28.4
- net I_3.3V-10: now also R59.2, U39.3, U41.4; no longer R81.2, U2.3, U37.4
- net I_3.3V-11: now also R58.2, U39.2; no longer R83.2, U2.2
- net I_3.3V-12: now also U36.4, U39.1; no longer U2.1, U39.4
- net I_3.3V-2: now also U50.3, U53.4; no longer U13.3, U29.4
- net I_3.3V-3: now also R73.2, U50.2, U51.4; no longer R124.2, U13.2, U30.4
- net I_3.3V-4: now also U49.4, U50.1; no longer U13.1, U31.4
- net I_3.3V-5: now also R70.2, U48.4, U50.20; no longer R126.2, U13.20, U32.4
- net I_3.3V-6: now also R67.2, U46.4, U50.19; no longer R70.2, U13.19, U33.4
- net I_3.3V-7: now also R65.2, U45.4, U50.18; no longer R72.2, U13.18, U34.4
- net I_3.3V-8: now also R63.2, U39.5, U43.4; no longer R74.2, U2.5, U35.4
- net I_3.3V-9: now also R60.2, U39.4, U42.4; no longer R78.2, U2.4, U36.4
- net I_3.3V-PV: now also R12.2, U23.5, U7.4; no longer R89.2, U52.4, U7.5
- net I_3.3V_IN-A: now also TP12.1, U31.6, U37.7; no longer TP15.1, U10.7, U22.6
- net I_3.3V_IN-A_N: now also R61.1-KELVIN, U31.5; no longer R5.1-KELVIN, U22.5
- net I_3.3V_IN-A_P: now also R61.2-KELVIN, U31.4; no longer R5.2-KELVIN, U22.4
- net I_3.3V_IN-B: now also TP43.1, U1.6, U2.8; no longer TP18.1, U25.6, U3.8
- net I_3.3V_IN-B_N: now also R11.1-KELVIN, U1.5; no longer R111.1-KELVIN, U25.5
- net I_3.3V_IN-B_P: now also R11.2-KELVIN, U1.4; no longer R111.2-KELVIN, U25.4
- net I_3.3V_OUT-A: now also TP15.1, U34.6, U37.8; no longer TP16.1, U10.8, U23.6
- net I_3.3V_OUT-A_N: now also R82.2-KELVIN, U34.5; no longer R41.2-KELVIN, U23.5
- net I_3.3V_OUT-A_P: now also R82.1-KELVIN, U34.4; no longer R41.1-KELVIN, U23.4
- net I_3.3V_OUT-B: now also TP42.1, U2.7, U6.6; no longer TP17.1, U24.6, U3.7
- net I_3.3V_OUT-B_N: now also R22.1-KELVIN, U6.5; no longer R15.1-KELVIN, U24.5
- net I_3.3V_OUT-B_P: now also R22.2-KELVIN, U6.4; no longer R15.2-KELVIN, U24.4
- net I_BATT-0: now also R56.2, U33.4, U39.20; no longer R11.2, U2.20, U40.4
- net I_BATT-1: now also R55.2, U32.4, U39.19; no longer R13.2, U2.19, U41.4
- net I_BATT-2: now also R54.2, U30.4, U39.18; no longer R43.2, U2.18, U42.4
- net I_BATT-3: now also R51.2, U23.1, U29.4; no longer R58.2, U43.4, U7.1
- net I_BATT-4: now also R50.2, U23.20, U28.4; no longer R59.2, U44.4, U7.20
- net I_BATT-5: now also R45.2, U23.19, U27.4; no longer R60.2, U45.4, U7.19
- net I_BATT-6: now also R39.2, U23.18, U25.4; no longer R63.2, U46.4, U7.18
- net I_BATT_IN-A: now also TP32.1, U10.6; no longer TP2.1, U8.6
- net I_BATT_IN-A_N: now also R2.1-KELVIN, U10.5; no longer R20.1-KELVIN, U8.5
- net I_BATT_IN-A_P: now also R2.2-KELVIN, U10.4; no longer R20.2-KELVIN, U8.4
- net I_BATT_IN-B: now also TP35.1, U13.6; no longer TP14.1, U21.6
- net I_BATT_IN-B_N: now also R7.2-KELVIN, U13.5; no longer R17.2-KELVIN, U21.5
- net I_BATT_IN-B_P: now also R7.1-KELVIN, U13.4; no longer R17.1-KELVIN, U21.4
- net I_BATT_OUT-A: now also TP8.1, U37.6, U44.6; no longer TP3.1, U10.6, U18.6
- net I_BATT_OUT-A_N: now also R1.1-KELVIN, U44.5; no longer R22.1-KELVIN, U18.5
- net I_BATT_OUT-A_P: now also R1.2-KELVIN, U44.4; no longer R22.2-KELVIN, U18.4
- net I_BATT_OUT-B: now also TP33.1, U11.6; no longer TP11.1, U19.6
- net I_BATT_OUT-B_N: now also R8.2-KELVIN, U11.5; no longer R16.2-KELVIN, U19.5
- net I_BATT_OUT-B_P: now also R8.1-KELVIN, U11.4; no longer R16.1-KELVIN, U19.4
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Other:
- board text added: "A"
- board text added: "B"

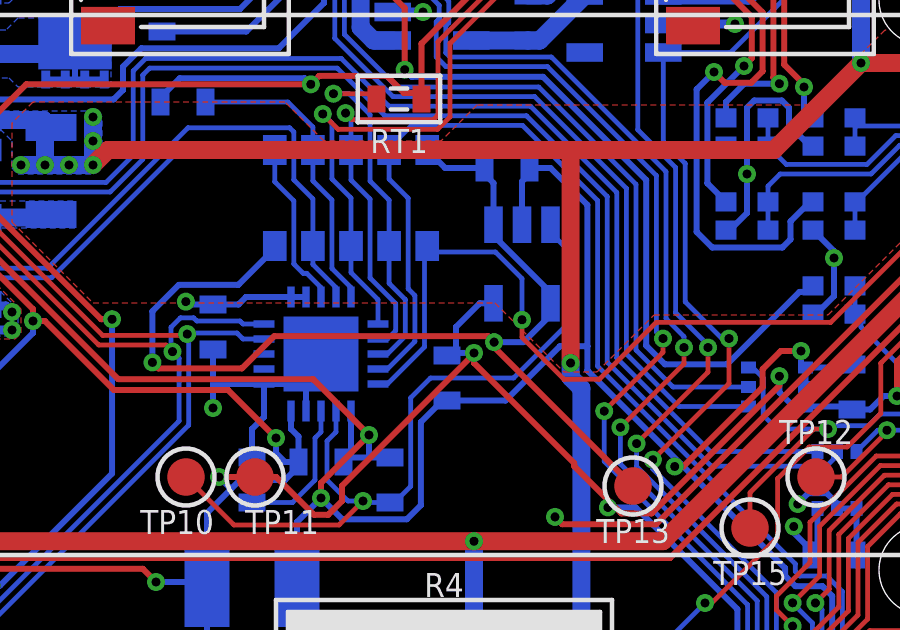
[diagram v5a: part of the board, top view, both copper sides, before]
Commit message: Removed pull up from current sense
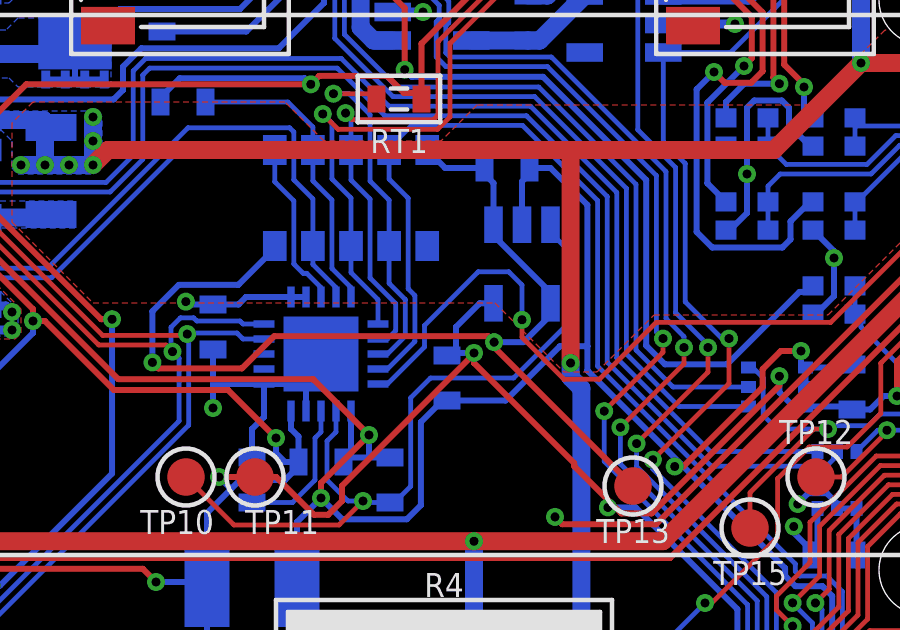
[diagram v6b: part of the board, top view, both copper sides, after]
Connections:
- net I_DEPLOY-0: no longer RN19.1
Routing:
- net I_DEPLOY-0: track 47.6 -> 45.2 mm
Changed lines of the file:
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@@
 <?xml version="1.0" encoding="utf-8"?>
 <!DOCTYPE eagle SYSTEM "eagle.dtd">
-<eagle version="9.4.2">
+<eagle version="9.5.1">
 <drawing>
 <settings>
@@
 <wire x1="72.89" y1="19.755" x2="67.075" y2="19.755" width="0.16" layer="1"/>
 <contactref element="U35" pad="5"/>
-<contactref element="RN19" pad="1"/>
-<wire x1="59.44" y1="22.3" x2="59.35" y2="22.21" width="0.16" layer="16"/>
-<wire x1="59.35" y1="18.935" x2="58.115" y2="17.7" width="0.16" layer="16"/>
-<wire x1="58.115" y1="17.7" x2="57.8" y2="17.7" width="0.16" layer="16"/>
-<wire x1="59.35" y1="22.21" x2="59.35" y2="18.935" width="0.16" layer="16"/>
-<wire x1="61.715" y1="22.1" x2="59.64" y2="22.1" width="0.16" layer="16"/>
-<wire x1="59.64" y1="22.1" x2="59.44" y2="22.3" width="0.16" layer="16"/>
-<wire x1="62.6" y1="19.84" x2="62.6" y2="21.215" width="0.16" layer="16"/>
-<wire x1="62.6" y1="21.215" x2="61.715" y2="22.1" width="0.16" layer="16"/>
+<wire x1="57.8" y1="17.7" x2="58.115" y2="17.7" width="0.16" layer="16"/>
+<wire x1="58.115" y1="17.7" x2="59.35" y2="18.935" width="0.16" layer="16"/>
+<wire x1="59.35" y1="18.935" x2="59.35" y2="19.65" width="0.16" layer="16"/>
+<wire x1="59.35" y1="19.65" x2="61.14" y2="21.44" width="0.16" layer="16"/>
+<wire x1="62.6" y1="21" x2="62.6" y2="19.84" width="0.16" layer="16"/>
+<wire x1="61.14" y1="21.44" x2="62.16" y2="21.44" width="0.16" layer="16"/>
+<wire x1="62.16" y1="21.44" x2="62.6" y2="21" width="0.16" layer="16"/>
 </signal>
 <signal name="!PC_DEPLOY-1">
